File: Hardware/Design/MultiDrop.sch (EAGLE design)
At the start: 35 parts

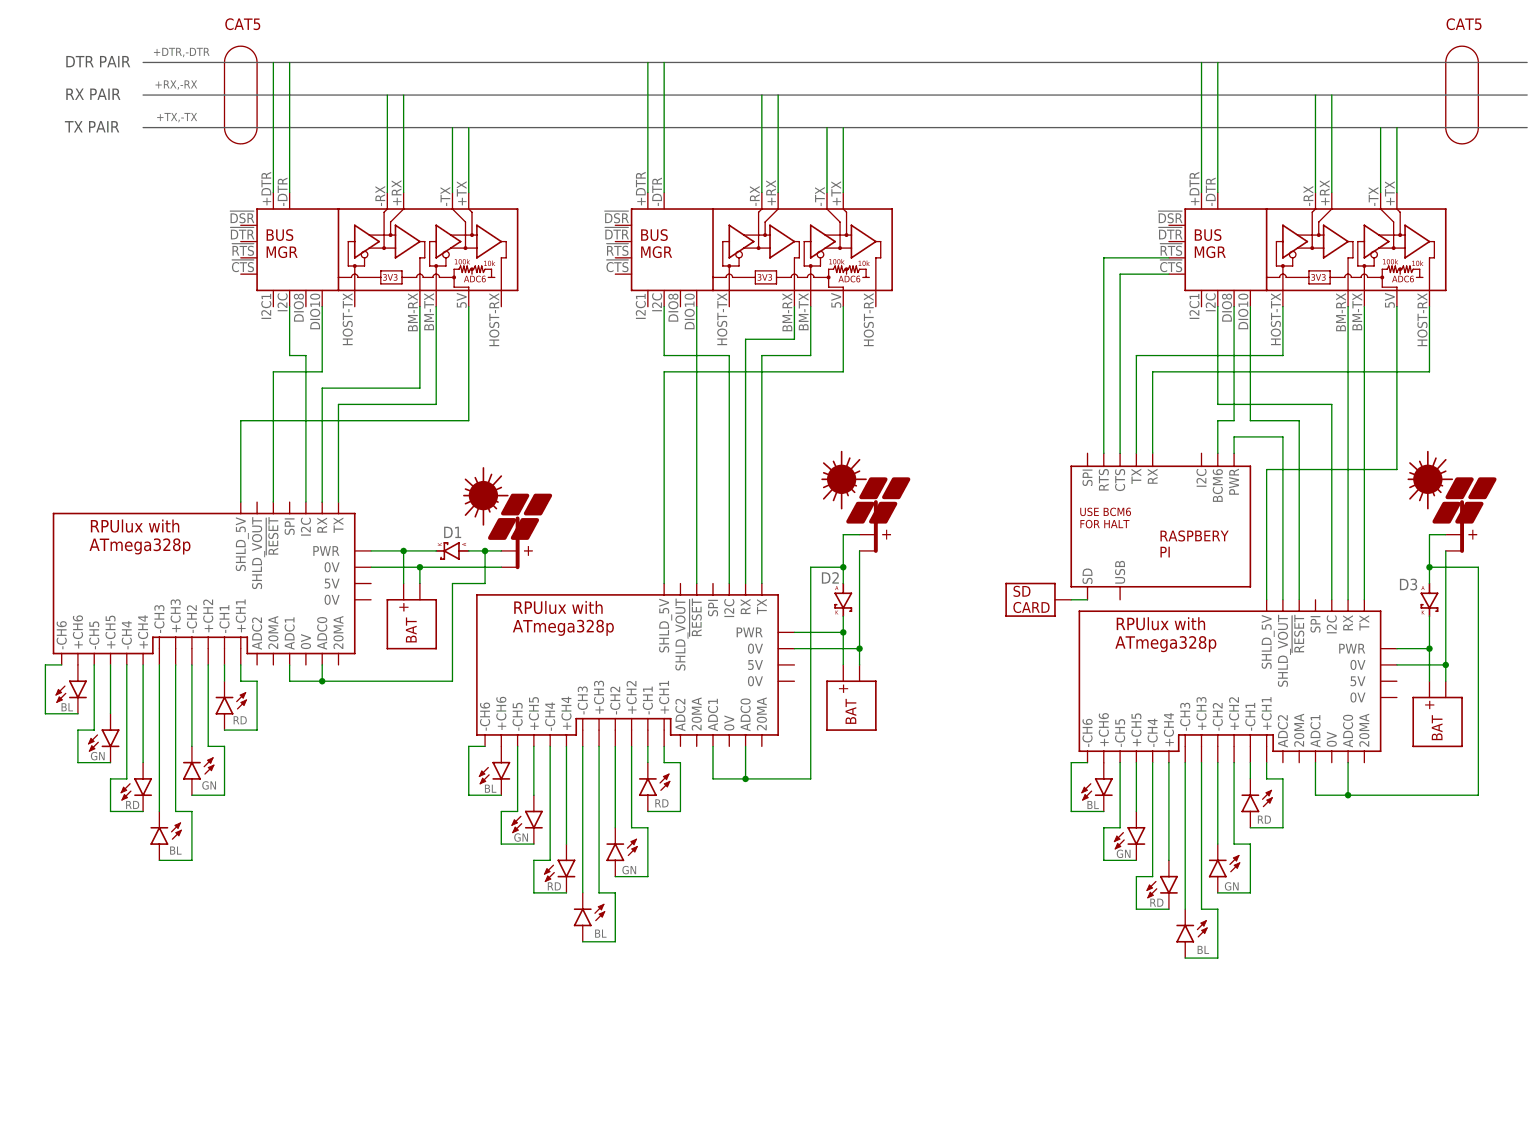
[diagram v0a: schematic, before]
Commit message: Alternat: check if the alt power input works
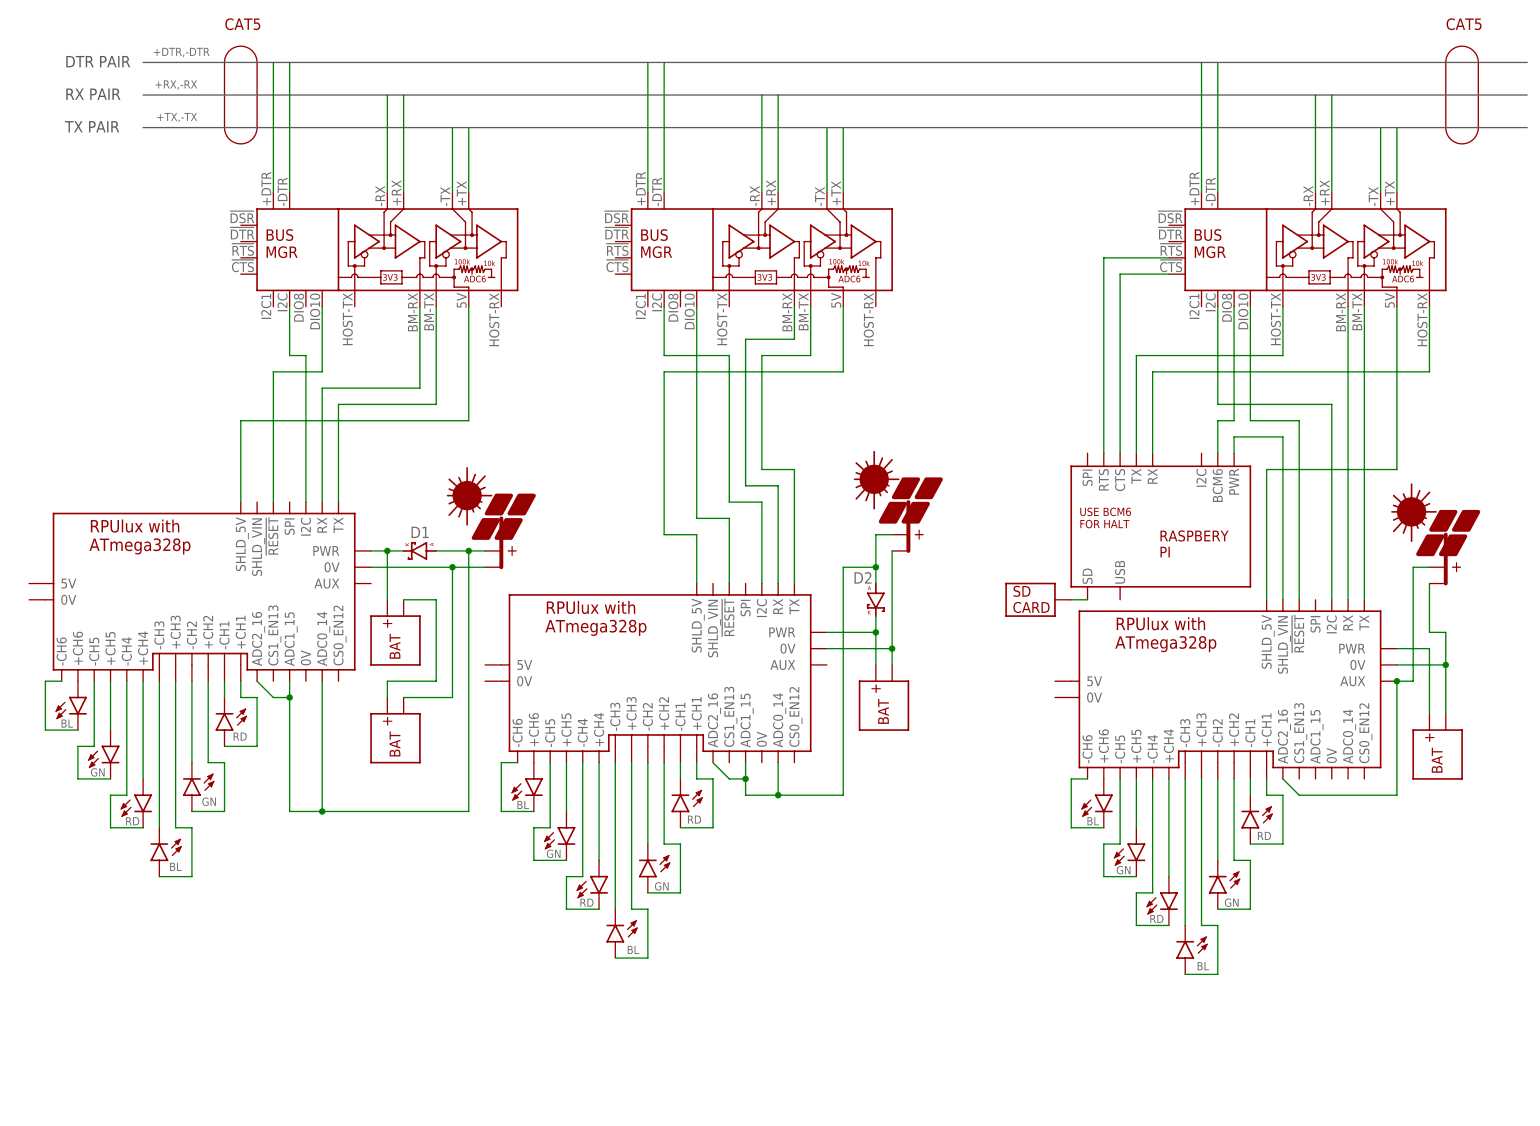
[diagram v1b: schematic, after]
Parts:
- removed D3: (no value), D-SBR:DSMB
- added U$11: BAT, Documentation:BAT
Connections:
- new net N$17: GN2.A, U$8.+CH6
- net N$1: now also U$8.TX; no longer U$6.TX
- net N$13: now also U$6.SHLD_5V; no longer U$8.SHLD_5V
- net N$14: now also U$6.TX; no longer U$8.TX
- net N$15: now also U$6.PWR; no longer D3.K, U$8.PWR
- net N$16: now also U$10.-BAT, U$11.+BAT; no longer D3.A, PV4.+PV, U$8.ADC0, U$8.ADC1
- net N$19: now also U$5.ADC0_14, U$5.ADC1_15, U$5.ADC2_16; no longer U$5.ADC0, U$5.ADC1
- net N$2: now also U$8.RX; no longer U$6.RX
- net N$20: now also U$8.-CH3; no longer U$6.-CH3
- net N$21: now also U$6.RX; no longer U$8.RX
- net N$24: now also U$8.+CH4; no longer U$6.+CH4
- net N$29: now also U$8.SHLD_5V; no longer U$6.SHLD_5V
- net N$3: now also U$8.ADC0_14, U$8.ADC1_15, U$8.ADC2_16; no longer U$6.ADC0, U$6.ADC1
- net N$30: now also U$8.!RESET; no longer U$6.!RESET
- net N$31: now also U$8.-CH4; no longer U$6.-CH4
- net N$32: now also U$6.I2C; no longer U$8.I2C
- net N$33: now also U$8.I2C; no longer U$6.I2C
- net N$34: now also U$8.+CH5; no longer U$6.+CH5
- net N$35: now also U$8.-CH5; no longer U$6.-CH5
- net N$36: now also GN3.A; no longer GN2.A
- net N$37: now also U$8.-CH6; no longer U$6.-CH6
- net N$38: now also U$11.-BAT, U$8.0V@2; no longer U$10.-BAT, U$6.0V@2
- net N$4: now also U$8.PWR; no longer U$6.PWR
- net N$40: no longer U$8.+CH4
- net N$41: now also U$6.SHLD_VIN; no longer U$8.SHLD_VOUT
- net N$42: now also U$6.0V@2; no longer U$8.0V@2
- net N$43: now also U$6.!RESET; no longer U$8.!RESET
- net N$46: no longer U$8.-CH4
- net N$47: no longer U$8.+CH5
- net N$49: no longer U$8.-CH5
- net N$5: now also U$8.-CH1; no longer U$6.-CH1
- net N$50: now also PV4.+PV, U$6.ADC2_16, U$6.AUX; no longer GN3.A, U$8.+CH6
- net N$51: no longer U$8.-CH6
- net N$6: now also U$8.+CH1; no longer U$6.+CH1
- net N$64: no longer U$8.-CH1
- net N$65: no longer U$8.+CH1
- net N$66: no longer U$8.+CH2
- net N$67: no longer U$8.-CH2
- net N$68: no longer U$8.+CH3
- net N$69: no longer U$8.-CH3
- net N$7: now also U$8.+CH2; no longer U$6.+CH2
- net N$8: now also U$8.-CH2; no longer U$6.-CH2
- net N$9: now also U$8.+CH3; no longer U$6.+CH3
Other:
- note added: "13AHr"
- note added: "40AHr EA"
- note added: "50AHr"
- note added: "SLP020-12U"
- note added: "SLP070-12U"
- note added: "SLP120-24U"
- moved on the sheet: D1, D2

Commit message: SelfTest: LED channels are running at half curr
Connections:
- net N$50: now also U$6.ALT; no longer U$6.AUX
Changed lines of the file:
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@@
 <segment>
 <pinref part="PV4" gate="G$1" pin="+PV"/>
-<pinref part="U$6" gate="G$1" pin="AUX"/>
+<pinref part="U$6" gate="G$1" pin="ALT"/>
 <wire x1="226.06" y1="7.62" x2="228.6" y2="7.62" width="0.1524" layer="91"/>
 <wire x1="228.6" y1="7.62" x2="228.6" y2="25.4" width="0.1524" layer="91"/>

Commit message: Arduino: fade example
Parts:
- removed B, GN2: BL, D-LED:LED5MM
- removed BL2, G: GN, D-LED:LED5MM
- removed D2: (no value), D-SBR:DSMB
- removed R, RD2: RD, D-LED:LED5MM
- added B3, B4, G3, G4, R10, R11, R12, R13, R14, R15, R16, R17, R18, R19, R20, R21, R22, R23, R24, R25, R26, R27, R28, R29, R3, R30, R31, R32, R33, R34, R35, R36, R37, R38, R39, R4, R40, R5, R6, R7, R8, R9: WH, D-LED:LED5MM
- added BL4, BL5: GN, D-LED:LED5MM
- added GN4, GN5: BL, D-LED:LED5MM
- added RD4, RD5: RD, D-LED:LED5MM
- added U$12: SSR_DC, Documentation:SSR_DC
- B1: value BL -> WH
- G1: value GN -> WH
- R1: value RD -> WH
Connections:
- new net N$100: R33.K, R37.A
- new net N$101: R34.K, R38.A
- new net N$102: R35.K, R39.A
- new net N$103: R36.K, R40.A
- new net N$104: R17.A, U$8.+CH3
- new net N$105: R37.K, U$8.-CH3
- new net N$106: R18.A, U$8.+CH4
- new net N$107: R38.K, U$8.-CH4
- new net N$108: R19.A, U$8.+CH5
- new net N$109: R39.K, U$8.-CH5
- new net N$110: R20.A, U$8.+CH6
- new net N$111: R40.K, U$8.-CH6
- new net N$56: R1.A, R3.K
- new net N$70: R3.A, R4.K
- new net N$71: G3.A, G4.K
- new net N$72: G1.A, G3.K
- new net N$73: B3.A, B4.K
- new net N$74: B1.A, B3.K
- new net N$75: GN1.K, GN4.A
- new net N$76: GN4.K, GN5.A
- new net N$77: BL1.K, BL4.A
- new net N$78: BL4.K, BL5.A
- new net N$79: RD1.K, RD4.A
- new net N$80: RD4.K, RD5.A
- new net N$81: PV2.+PV, U$12.+DC, U$12.+IN, U$5.ADC2_16
- new net N$82: U$12.-IN, U$5.ADC0_14
- new net N$83: R17.K, R21.A
- new net N$84: R18.K, R22.A
- new net N$85: R19.K, R23.A
- new net N$86: R9.K, U$8.-CH1
- new net N$87: R20.K, R24.A
- new net N$88: R21.K, R25.A
- new net N$89: R22.K, R26.A
- new net N$90: R23.K, R27.A
- new net N$91: R24.K, R28.A
- new net N$92: R25.K, R29.A
- new net N$93: R26.K, R30.A
- new net N$94: R27.K, R31.A
- new net N$95: R28.K, R32.A
- new net N$96: R29.K, R33.A
- new net N$97: R30.K, R34.A
- new net N$98: R31.K, R35.A
- new net N$99: R32.K, R36.A
- net N$17: now also R7.A, R8.K; no longer GN2.A, U$8.+CH6
- net N$18: now also U$12.-DC; no longer D2.K
- net N$19: now also R11.A, R12.K; no longer D2.A, PV2.+PV, U$5.ADC0_14, U$5.ADC1_15, U$5.ADC2_16
- net N$20: now also R12.A, R13.K; no longer B.K, U$8.-CH3
- net N$24: now also R13.A, R14.K; no longer RD2.A, U$8.+CH4
- net N$31: now also R14.A, R15.K; no longer RD2.K, U$8.-CH4
- net N$34: now also R15.A, R16.K; no longer BL2.A, U$8.+CH5
- net N$35: now also R16.A, U$8.+CH2; no longer BL2.K, U$8.-CH5
- net N$37: now also R11.K, U$8.-CH2; no longer GN2.K, U$8.-CH6
- net N$5: now also R10.A, R5.K; no longer R.K, U$8.-CH1
- net N$53: now also RD5.K; no longer RD1.K
- net N$55: now also BL5.K; no longer BL1.K
- net N$57: now also GN5.K; no longer GN1.K
- net N$59: now also R4.A; no longer R1.A
- net N$6: now also R8.A; no longer R.A
- net N$60: now also G4.A; no longer G1.A
- net N$62: now also B4.A; no longer B1.A
- net N$7: now also R10.K, R9.A; no longer G.A, U$8.+CH2
- net N$8: now also R5.A, R6.K; no longer G.K, U$8.-CH2
- net N$9: now also R6.A, R7.K; no longer B.A, U$8.+CH3
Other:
- moved on the sheet: D1

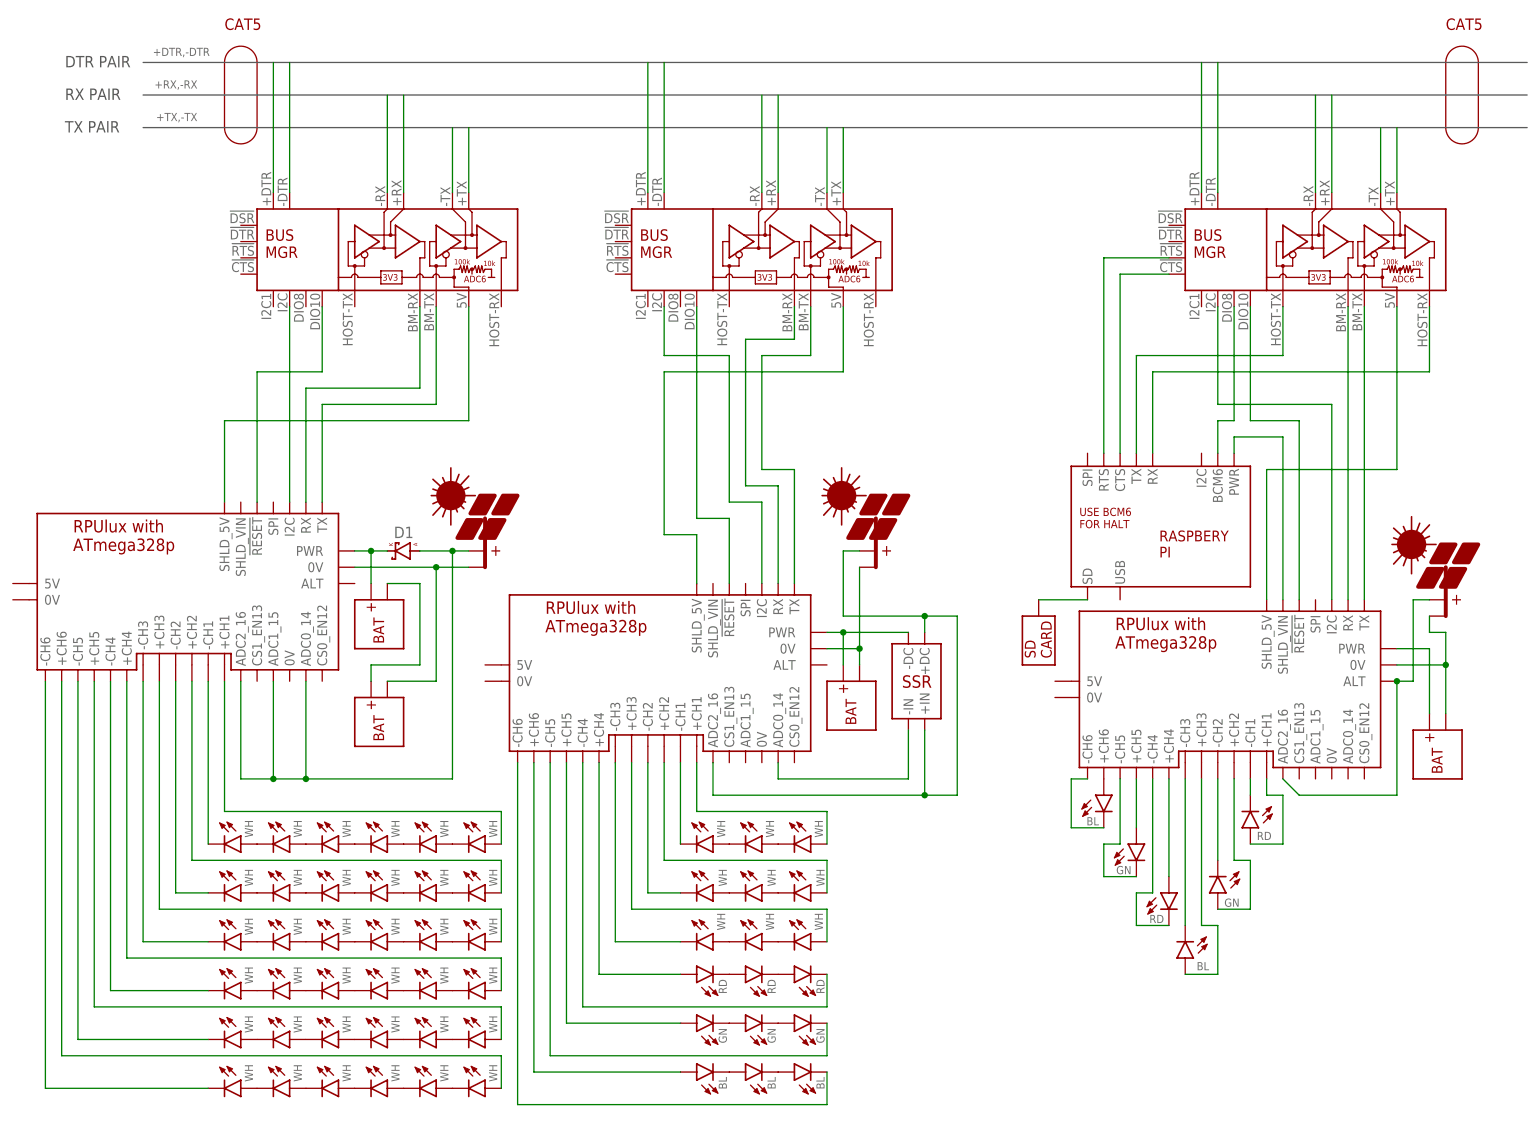
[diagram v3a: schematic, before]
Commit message: Hardware: ^1 evaluation, work around to get 330mA on led channels
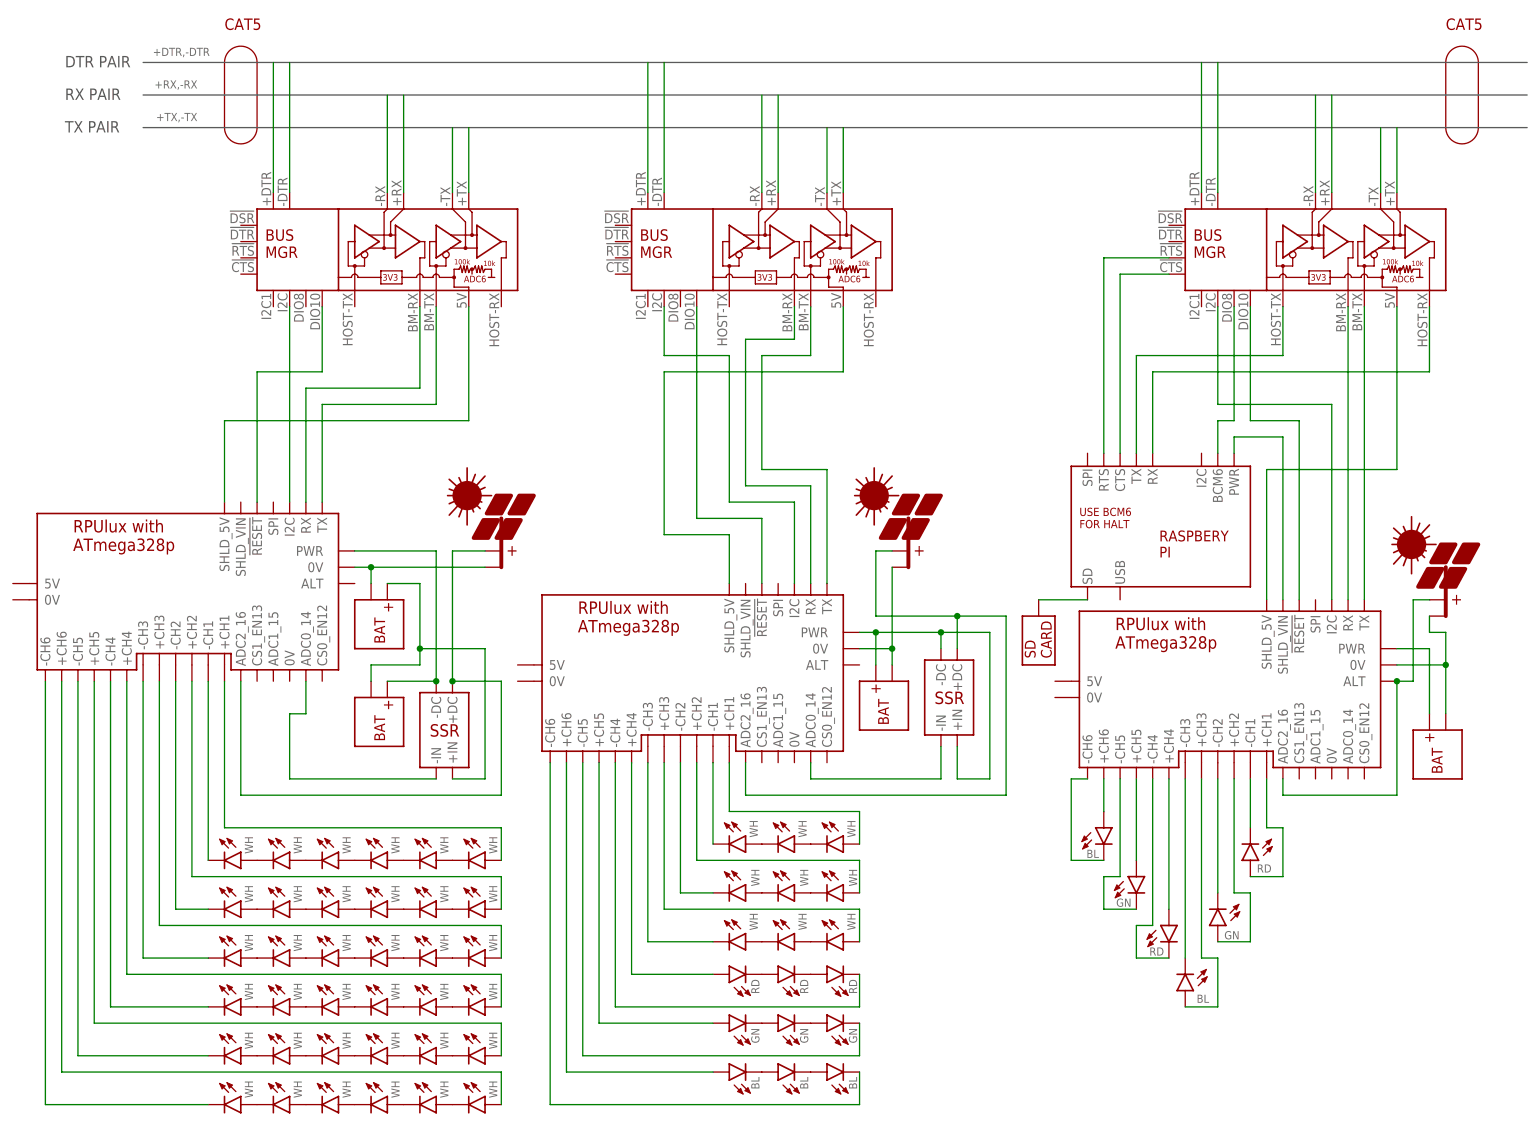
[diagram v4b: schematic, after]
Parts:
- removed D1: (no value), D-SBR:DSMB
- added U$13: SSR_DC, Documentation:SSR_DC
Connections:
- removed net N$4: D1.K, U$10.+BAT, U$8.PWR
- new net N$112: PV1.-PV, U$10.-BAT, U$8.0V@2
- new net N$113: U$13.-IN, U$8.ADC0_14
- net N$16: now also U$10.+BAT, U$11.-BAT, U$13.+IN; no longer U$10.-BAT, U$11.+BAT
- net N$18: now also U$12.+IN
- net N$3: now also U$13.+DC; no longer D1.A, U$8.ADC0_14, U$8.ADC1_15
- net N$38: now also U$11.+BAT, U$13.-DC, U$8.PWR; no longer PV1.-PV, U$11.-BAT, U$8.0V@2
- net N$81: no longer U$12.+IN
